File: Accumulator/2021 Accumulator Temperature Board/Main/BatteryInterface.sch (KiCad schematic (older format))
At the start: 2 parts

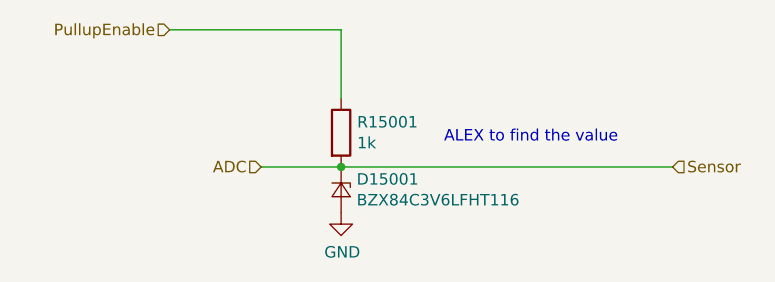
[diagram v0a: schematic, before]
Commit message: Changes to Thermoboard
Disconnected mounting holes from GND, changed Zener package to hand-soldering.
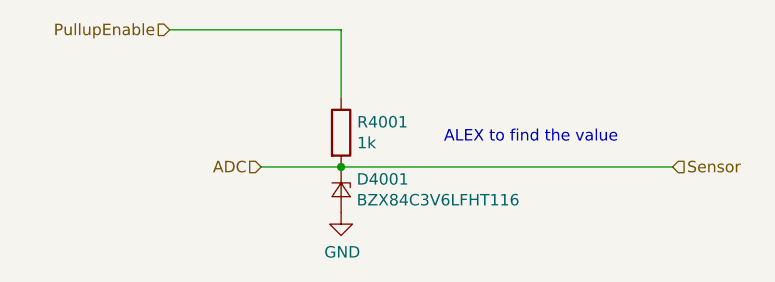
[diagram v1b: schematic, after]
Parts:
- D4001: footprint Diode_SMD:D_SOD-323 -> Diode_SMD:D_SOD-323_HandSoldering
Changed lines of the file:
@@
 $Descr A4 11693 8268
 encoding utf-8
-Sheet 11 16
+Sheet 5 16
 Title ""
 Date ""
@@
 AR Path="/5C176383/5C19D9D8/5C19D145" Ref="R14001"  Part="1"
 AR Path="/5C176383/5C19D9DD/5C19D145" Ref="R15001"  Part="1"
-F 0 "R15001" H 3670 2296 50  0000 L CNN
+F 0 "R4001" H 3670 2296 50  0000 L CNN
 F 1 "1k" H 3670 2205 50  0000 L CNN
 F 2 "Resistor_SMD:R_0805_2012Metric_Pad1.15x1.40mm_HandSolder" V 3530 2250 50  0001 C CNN
@@
 AR Path="/5C176383/5C19D9D8/5C19D4DE" Ref="D14001"  Part="1"
 AR Path="/5C176383/5C19D9DD/5C19D4DE" Ref="D15001"  Part="1"
-F 0 "D15001" V 3554 2568 50  0000 L CNN
+F 0 "D4001" V 3554 2568 50  0000 L CNN
 F 1 "BZX84C3V6LFHT116" V 3645 2568 50  0000 L CNN
-F 2 "Diode_SMD:D_SOD-323" V 3600 2500 50  0001 C CNN
+F 2 "Diode_SMD:D_SOD-323_HandSoldering" V 3600 2500 50  0001 C CNN
 F 3 "~" V 3600 2500 50  0001 C CNN
 	1    3600 2500
@@
 AR Path="/5C176383/5C19D9D8/5C19D542" Ref="#PWR0133"  Part="1"
 AR Path="/5C176383/5C19D9DD/5C19D542" Ref="#PWR0135"  Part="1"
-F 0 "#PWR0135" H 3600 2350 50  0001 C CNN
+F 0 "#PWR0113" H 3600 2350 50  0001 C CNN
 F 1 "GND" H 3605 2427 50  0000 C CNN
 F 2 "" H 3600 2600 50  0001 C CNN

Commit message: Changes to Thermoboard Mounting
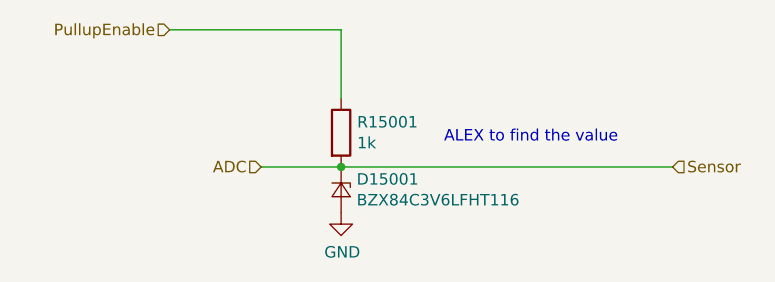
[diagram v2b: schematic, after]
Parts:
- D4001: footprint Diode_SMD:D_SOD-323_HandSoldering -> Diode_SMD:D_SOD-323
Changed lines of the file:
@@
 $Descr A4 11693 8268
 encoding utf-8
-Sheet 5 16
+Sheet 11 16
 Title ""
 Date ""
@@
 AR Path="/5C176383/5C19D9D8/5C19D145" Ref="R14001"  Part="1"
 AR Path="/5C176383/5C19D9DD/5C19D145" Ref="R15001"  Part="1"
-F 0 "R4001" H 3670 2296 50  0000 L CNN
+F 0 "R15001" H 3670 2296 50  0000 L CNN
 F 1 "1k" H 3670 2205 50  0000 L CNN
 F 2 "Resistor_SMD:R_0805_2012Metric_Pad1.15x1.40mm_HandSolder" V 3530 2250 50  0001 C CNN
@@
 AR Path="/5C176383/5C19D9D8/5C19D4DE" Ref="D14001"  Part="1"
 AR Path="/5C176383/5C19D9DD/5C19D4DE" Ref="D15001"  Part="1"
-F 0 "D4001" V 3554 2568 50  0000 L CNN
+F 0 "D15001" V 3554 2568 50  0000 L CNN
 F 1 "BZX84C3V6LFHT116" V 3645 2568 50  0000 L CNN
-F 2 "Diode_SMD:D_SOD-323_HandSoldering" V 3600 2500 50  0001 C CNN
+F 2 "Diode_SMD:D_SOD-323" V 3600 2500 50  0001 C CNN
 F 3 "~" V 3600 2500 50  0001 C CNN
 	1    3600 2500
@@
 AR Path="/5C176383/5C19D9D8/5C19D542" Ref="#PWR0133"  Part="1"
 AR Path="/5C176383/5C19D9DD/5C19D542" Ref="#PWR0135"  Part="1"
-F 0 "#PWR0113" H 3600 2350 50  0001 C CNN
+F 0 "#PWR0135" H 3600 2350 50  0001 C CNN
 F 1 "GND" H 3605 2427 50  0000 C CNN
 F 2 "" H 3600 2600 50  0001 C CNN
